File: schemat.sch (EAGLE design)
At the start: 34 parts, among them Q1-1 IRFBG30, Q1-2 IRFBG30, Q1-3 IRFBG30, Q2-1 IRFBG30, Q2-2 IRFBG30, Q2-3 IRFBG30, Q3-1 IRFBG30, Q3-2 IRFBG30, Q3-3 IRFBG30, Q4-1 IRFBG30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

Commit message: schematic ready
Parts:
- added AUDIO: PIN1-2, con-faston:PIN1-2
- added C8: 100n, 100n:0402B104K250CT
- added C9: 10u, 10u:ECEA1EKS100
- added GND26: GND, con-faston:PIN1-2
- added IC1: LM358N, linear:LM358N
- added POT2, POT3: (no value), rcl:R-TRIMM64W
- added R7: 1k, rcl:R-EU_0204/7
- added R8: 10k, rcl:R-EU_0204/7
- C1, C4: device rcl:CPOL-EUE10-25 -> 6_3x11:35ZLH100MEFC6.3X11
- C2, C5: device rcl:CPOL-EUE10-25 -> 10u:ECEA1EKS100
- C3, C6: device rcl:CPOL-EUE10-25 -> 100n:0402B104K250CT
- R1, R2, R3, R4, R5, R6: device rcl:R-EU_0207/10 -> rcl:R-EU_0204/7
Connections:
- removed net S2: Q2-1.G, Q2-2.G, Q2-3.G
- removed net S3: Q3-1.G, Q3-2.G, Q3-3.G
- removed net S4: Q4-1.G, Q4-2.G, Q4-3.G
- new net 12V_DRV: C4.1, C5.1, C6.1, L1.2
- new net 12V_DRV1: C8.1, IC1A.+IN, POT3.S
- new net N$10: IC1A.-IN, POT2.E, R7.1
- new net N$11: AUDIO.1, C9.2, R8.2
- new net N$12: GND26.1, R8.1
- new net N$7: R6.1, U4.OUT
- new net N$8: IC1A.OUT, POT2.A, U2+U3.INB+
- new net N$9: C9.1, R7.2
- net 12V: now also C1.1, C2.1, C3.1; no longer C1.+, C2.+, C3.+
- net GND: now also C1.2, C2.2, C3.2, C4.2, C5.2, C6.2, C8.2, POT3.E, U4.GND, U4.GND_2; no longer C1.-, C2.-, C3.-, C4.-, C5.-, C6.-
- net S1: now also Q2-1.G, Q2-2.G, Q2-3.G, Q3-1.G, Q3-2.G, Q3-3.G, Q4-1.G, Q4-2.G, Q4-3.G, R6.2
- net VCC: now also POT3.A, U4.VS, U4.VS_2; no longer C4.+, C5.+, C6.+, L1.2
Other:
- moved on the sheet: R6

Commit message: project finished
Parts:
- removed IC1: LM358N, linear:LM358N
- added IC2: LM321MF, linear:LM321MF
- added SECONDARY_GND: GND, con-faston:PIN1-2
- renumbered GND26 to GND_AUDIO
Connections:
- removed net N$12: GND_AUDIO.1, R8.1
- removed net VCC: L1.1, POT3.A, R2.2, U2+U3.VDD, U4.VS, U4.VS_2
- new net 5V: C2.1, C3.1, IC2.V+, POT3.A, R2.2, U1.OUT, U2+U3.VDD
- net 12V: now also L1.1; no longer C2.1, C3.1, U1.OUT
- net 12V_DRV: now also U4.VS, U4.VS_2
- net 12V_DRV1: now also IC2.+IN; no longer IC1A.+IN
- net GND: now also GND_AUDIO.1, IC2.V-, R8.1, SECONDARY_GND.1
- net N$10: now also IC2.-IN; no longer IC1A.-IN
- net N$8: now also IC2.OUT; no longer IC1A.OUT

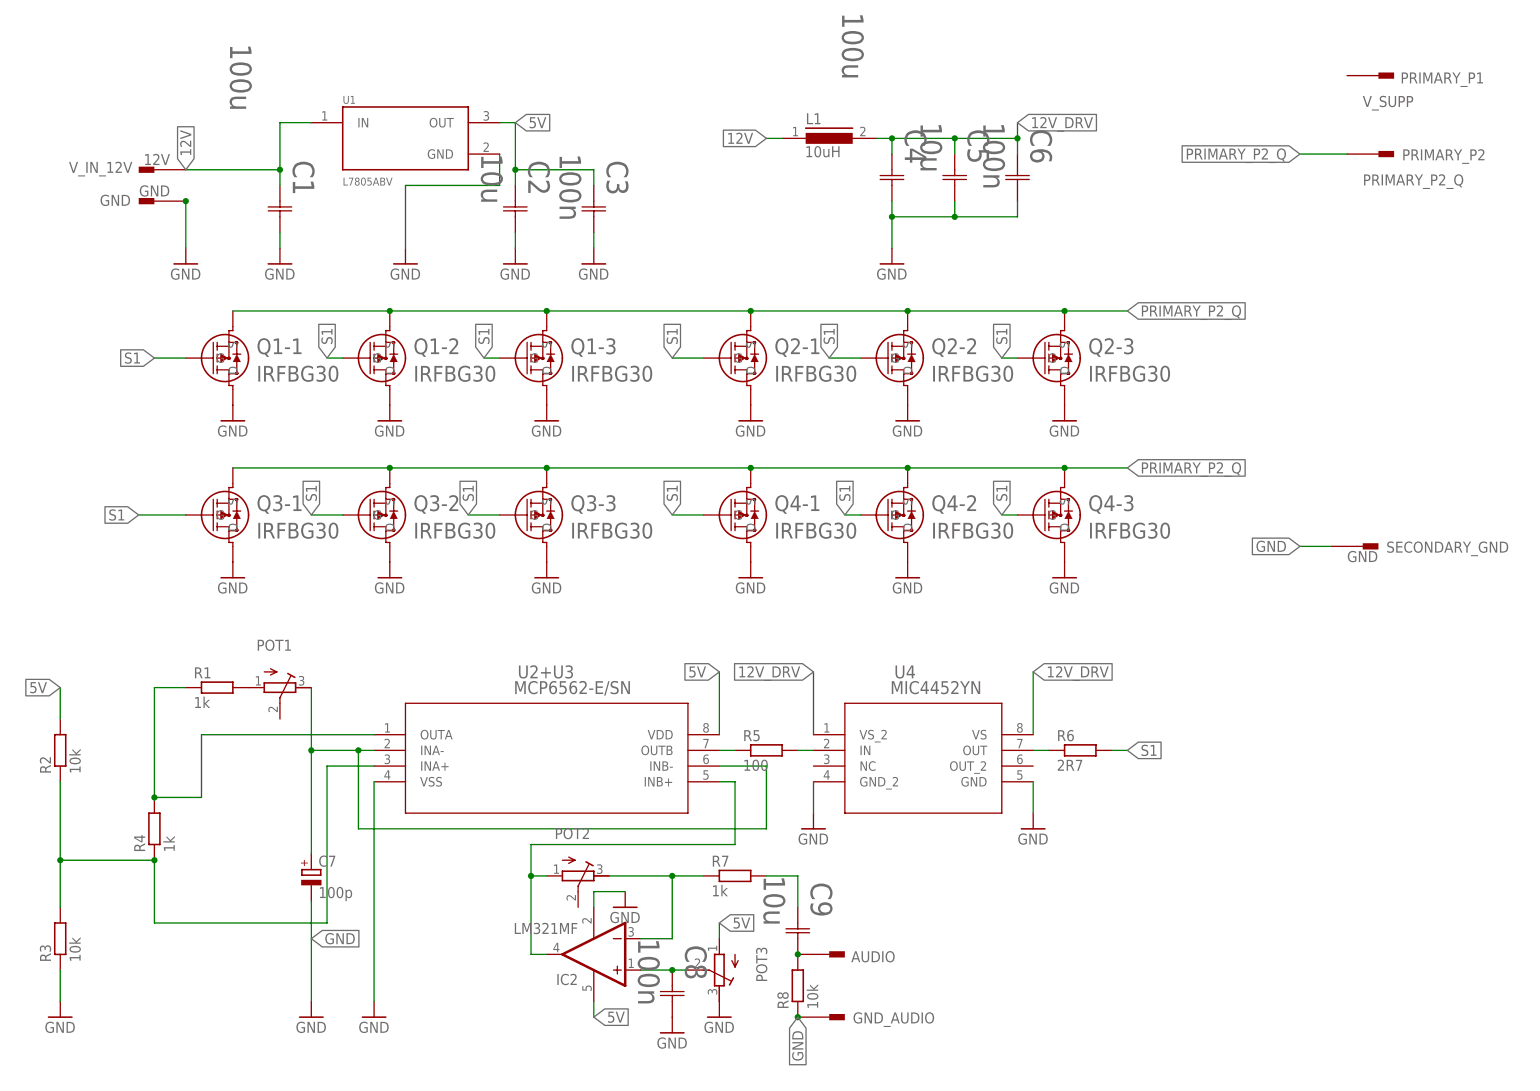
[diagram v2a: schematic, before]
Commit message: transistor changed
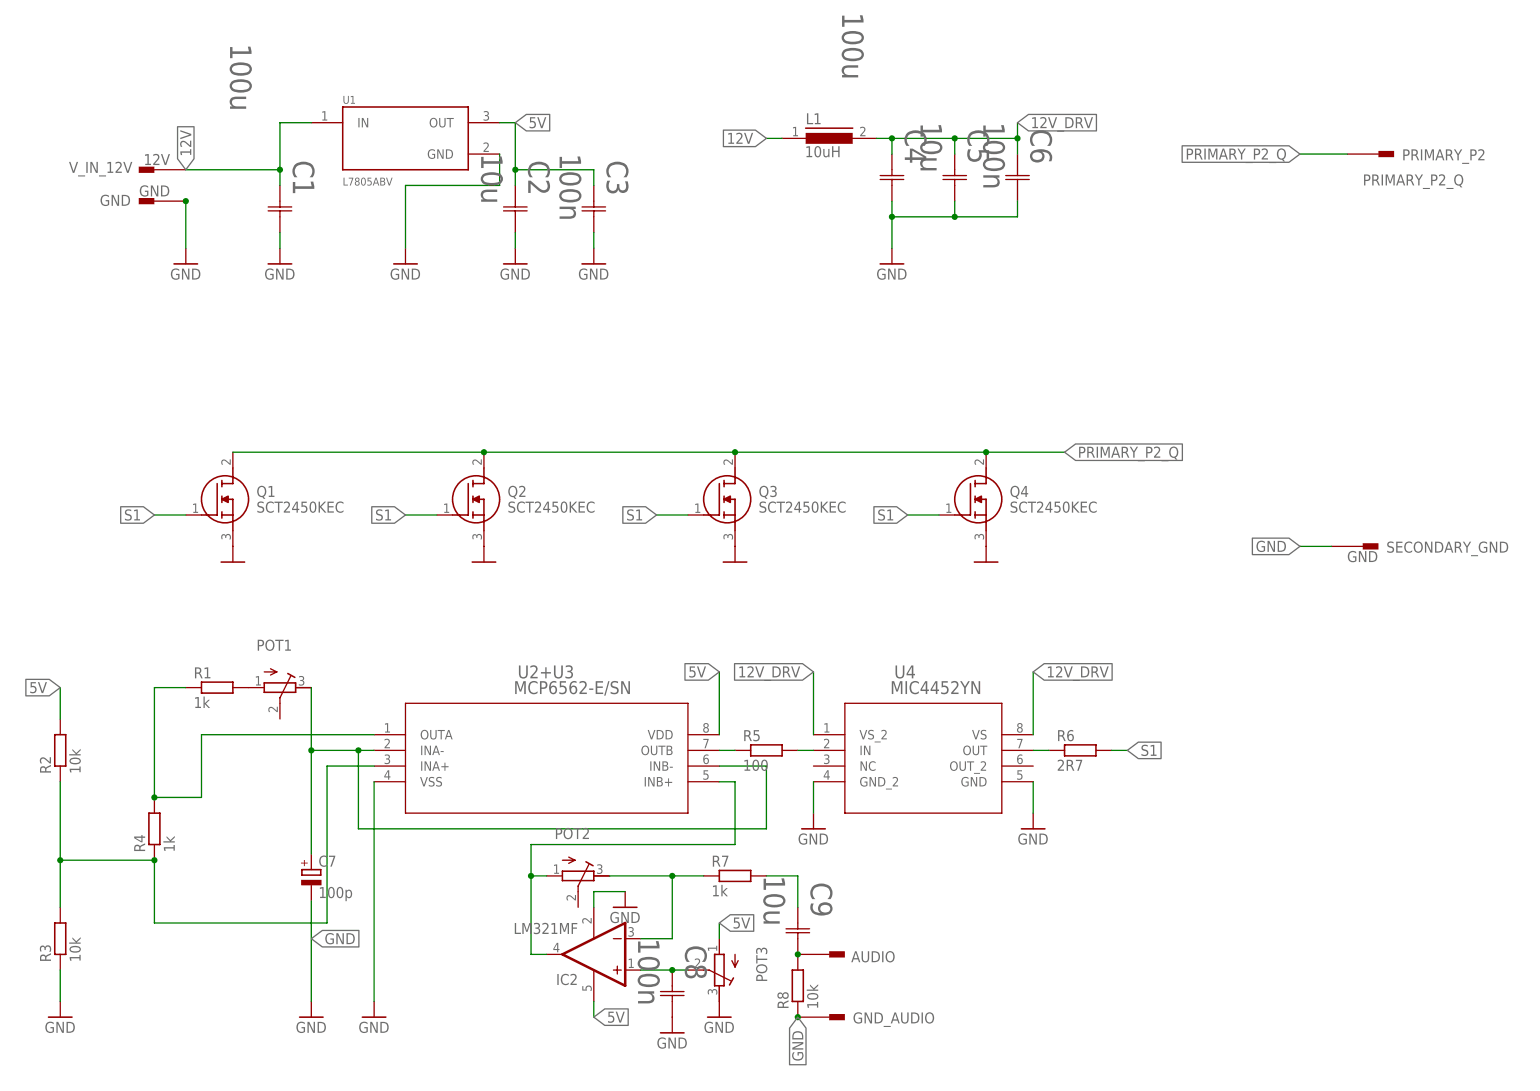
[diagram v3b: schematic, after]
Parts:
- removed PRIMARY_P1: V_SUPP, con-faston:PIN1-2
- removed Q1-1, Q1-2, Q1-3, Q2-1, Q2-2, Q2-3, Q3-1, Q3-2, Q3-3, Q4-1, Q4-2, Q4-3: IRFBG30, IRFBG30:IRFBG30
- added Q1, Q2, Q3, Q4: SCT2450KEC, SCT2450KEC:SCT2450KEC
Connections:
- net GND: now also Q1.S, Q2.S, Q3.S, Q4.S; no longer Q1-1.D, Q1-2.D, Q1-3.D, Q2-1.D, Q2-2.D, Q2-3.D, Q3-1.D, Q3-2.D, Q3-3.D, Q4-1.D, Q4-2.D, Q4-3.D
- net PRIMARY_P2_Q: now also Q1.D, Q2.D, Q3.D, Q4.D; no longer Q1-1.S, Q1-2.S, Q1-3.S, Q2-1.S, Q2-2.S, Q2-3.S, Q3-1.S, Q3-2.S, Q3-3.S, Q4-1.S, Q4-2.S, Q4-3.S
- net S1: now also Q1.G, Q2.G, Q3.G, Q4.G; no longer Q1-1.G, Q1-2.G, Q1-3.G, Q2-1.G, Q2-2.G, Q2-3.G, Q3-1.G, Q3-2.G, Q3-3.G, Q4-1.G, Q4-2.G, Q4-3.G
